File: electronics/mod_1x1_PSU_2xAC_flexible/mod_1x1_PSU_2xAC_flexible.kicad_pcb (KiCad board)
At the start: 2 copper layers, 42.5 x 46.2 mm, 56 parts, among them J1 module_2x15_left_input, J2 module_2x15_right_input, J3 Jack-DC, J4 Jack-DC, J5 Conn_01x02, J6 Conn_01x02, U1 LM317, U2 LM317, U3 LM337, U4 LM78XX

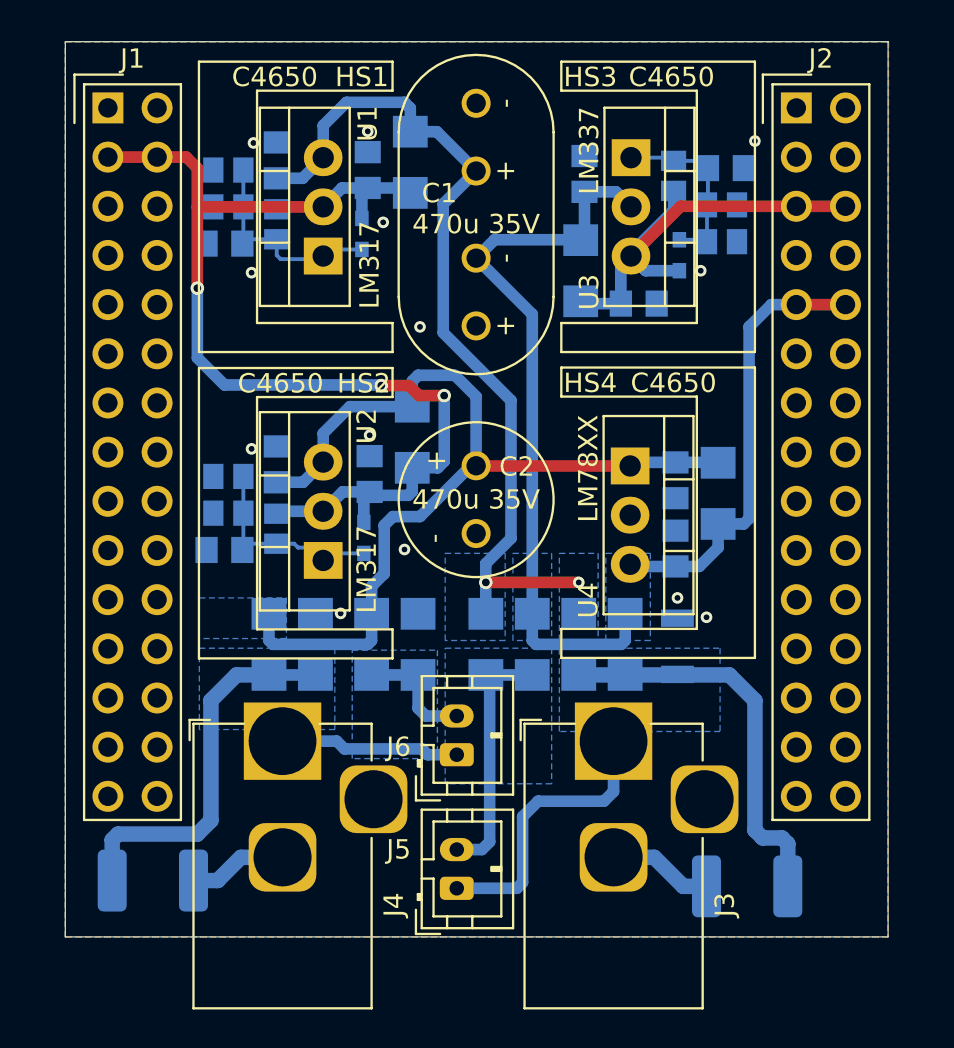
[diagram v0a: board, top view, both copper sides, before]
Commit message: updated PCB with newer/different footprints
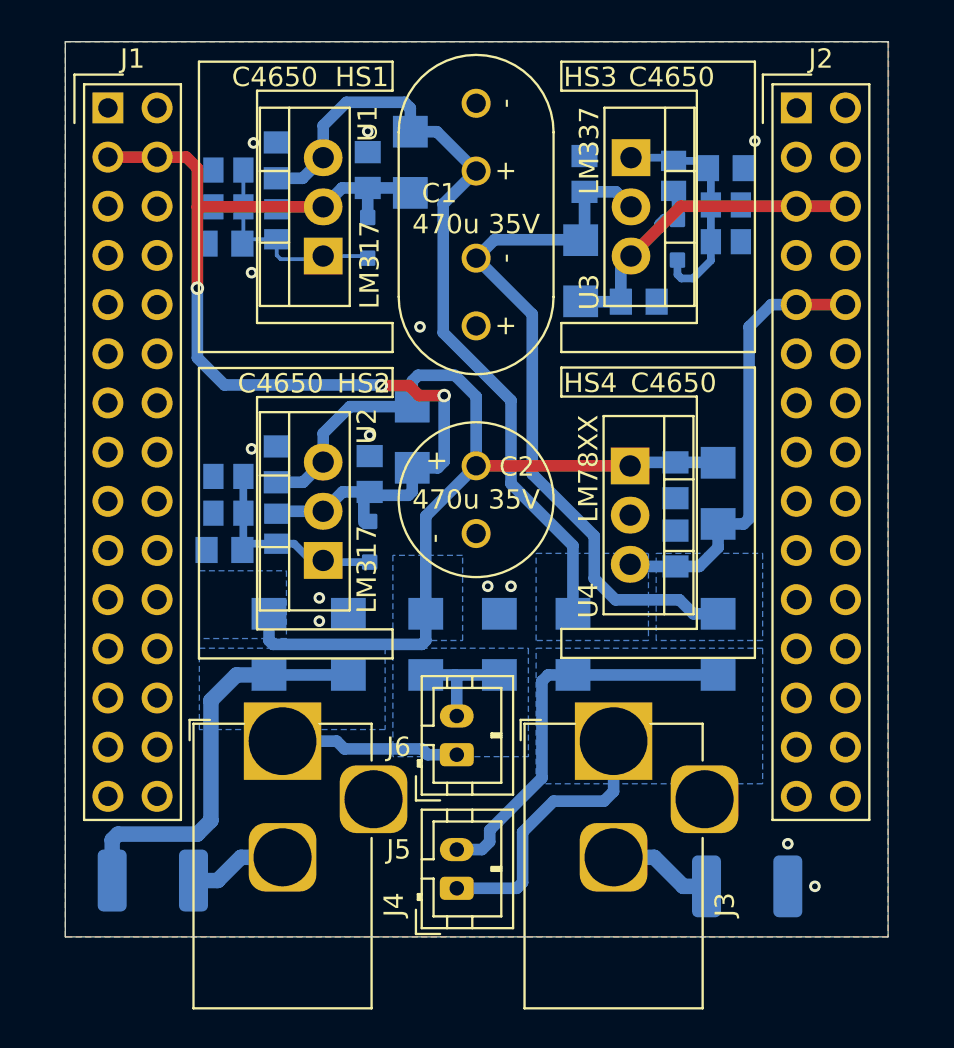
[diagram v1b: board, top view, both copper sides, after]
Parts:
- removed D3, D4: D, SquantorDiodes:SOD-123F-hand
- removed R1: R, SquantorRcl:R_1206
- D10, D12, D14: footprint SquantorDiodes:SOD-523_hand -> SquantorDiodes:SOD-323-nexperia-hand
- N1: value 20220716 -> 202200917
- moved D2 9.60 mm to (176.3, 100.1)
- moved D1 4.50 mm to (168.8, 100.1)
- moved D6 4.20 mm to (165.0, 100.1)
- moved D5 2.80 mm to (161.2, 100.1)
- moved D8 1.70 mm to (157.2, 100.1)
- moved D12 0.81 mm to (174.2, 79.2), turned to 90 degrees
- moved D14 0.36 mm to (158.3, 94.8)
- moved D10 0.36 mm to (158.2, 79.1)
- moved R5 0.20 mm to (176.7, 77.4)
- moved R6 0.20 mm to (176.7, 79.3)
- moved C11 0.10 mm to (172.2, 82.4)
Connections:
- F2 pad 2: /AC1_NEUT -> GND
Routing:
- net /AC1_NEUT: track 20.5 -> 0.00 mm
- net /AC1_PHASE: track 13.0 -> 20.5 mm
- net /DC1p: track 45.4 -> 41.4 mm, vias 2 -> 0
- net Net-(D12-K): track 9.49 -> 12.0 mm
- net /V-A: track 24.0 -> 21.6 mm
- net /AC2_NEUT: track 19.8 -> 21.5 mm
- net /DC1n: track 38.4 -> 37.3 mm
- net /DC2: track 50.0 -> 50.6 mm
- removed copper zone on B.Cu, net /AC1_NEUT

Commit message: small changes for producability and form and fit
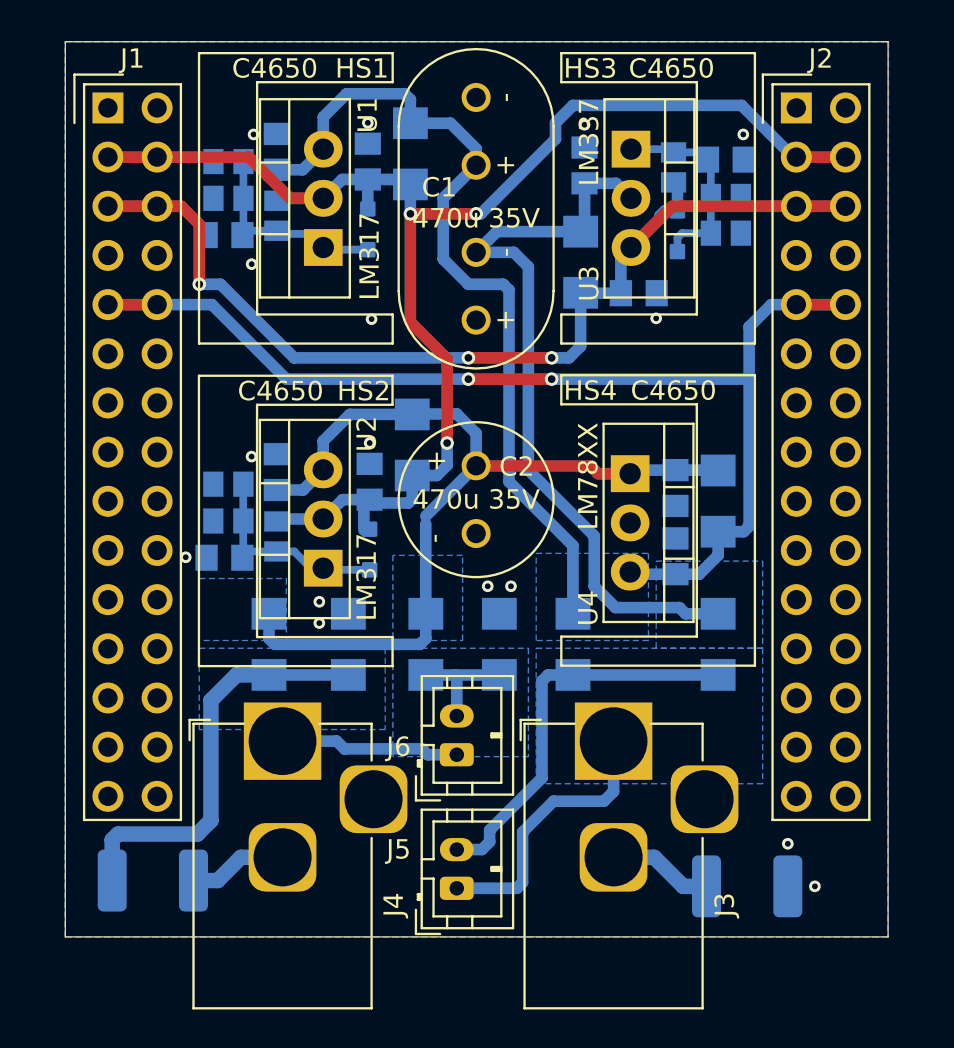
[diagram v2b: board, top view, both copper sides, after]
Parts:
- N1: value 202200917 -> 202201025
- moved C4 0.44 mm to (150.8, 79.0)
- moved R4 0.44 mm to (153.5, 78.0)
- moved C9 0.44 mm to (158.2, 75.2)
- moved D10 0.44 mm to (158.2, 78.7)
- moved HS1 0.44 mm to (154.5, 77.1)
- moved C3 0.44 mm to (153.5, 74.7)
- moved D9 0.44 mm to (160.4, 74.8)
- moved R2 0.44 mm to (151.0, 77.1)
- moved R3 0.44 mm to (151.0, 75.2)
- moved U1 0.44 mm to (155.9, 77.1)
- moved C11 0.44 mm to (172.2, 82.0)
- moved R5 0.44 mm to (176.7, 77.0)
- moved R7 0.44 mm to (174.0, 75.5)
- moved C5 0.44 mm to (169.4, 75.4)
- moved C6 0.44 mm to (176.7, 75.1)
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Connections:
- J1 pad 10: unconnected-(J1-+5V-Pad10) -> /+5V
- J1 pad 5: unconnected-(J1--VA-Pad5) -> /V-A
- J1 pad 6: unconnected-(J1--VA-Pad6) -> /V-A
- J1 pad 9: unconnected-(J1-+5V-Pad9) -> /+5V
- J2 pad 3: unconnected-(J2-+VA-Pad3) -> /V+A
- J2 pad 4: unconnected-(J2-+VA-Pad4) -> /V+A
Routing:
- net /+5V: track 23.3 -> 58.4 mm, vias 0 -> 2
- net /V-A: track 21.6 -> 53.9 mm, vias 0 -> 3
- net /V+A: track 59.4 -> 75.2 mm
- net /DC2: track 50.6 -> 46.5 mm
- net /DC1p: track 41.4 -> 43.7 mm
- net /DC1n: track 37.3 -> 39.4 mm
- net Net-(D12-K): track 12.0 -> 10.6 mm
- net Net-(D10-A): track 11.4 -> 10.8 mm
- net GND: vias 13 -> 16

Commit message: updated components and fixed warnings
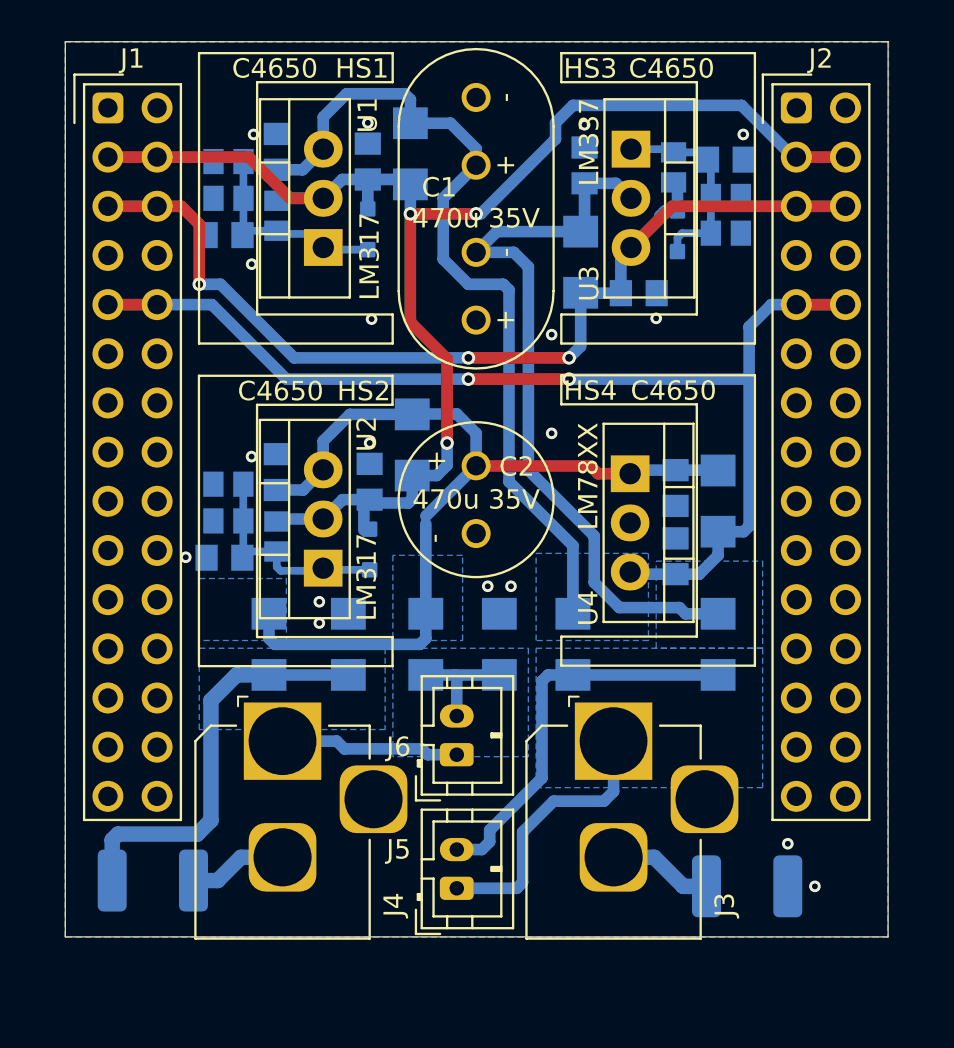
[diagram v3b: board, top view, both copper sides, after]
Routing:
- net Net-(D14-A): track 10.9 -> 11.5 mm
- net GND: vias 16 -> 18

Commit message: imported aisler budget design rules, fixed all DRC errors resulting from that
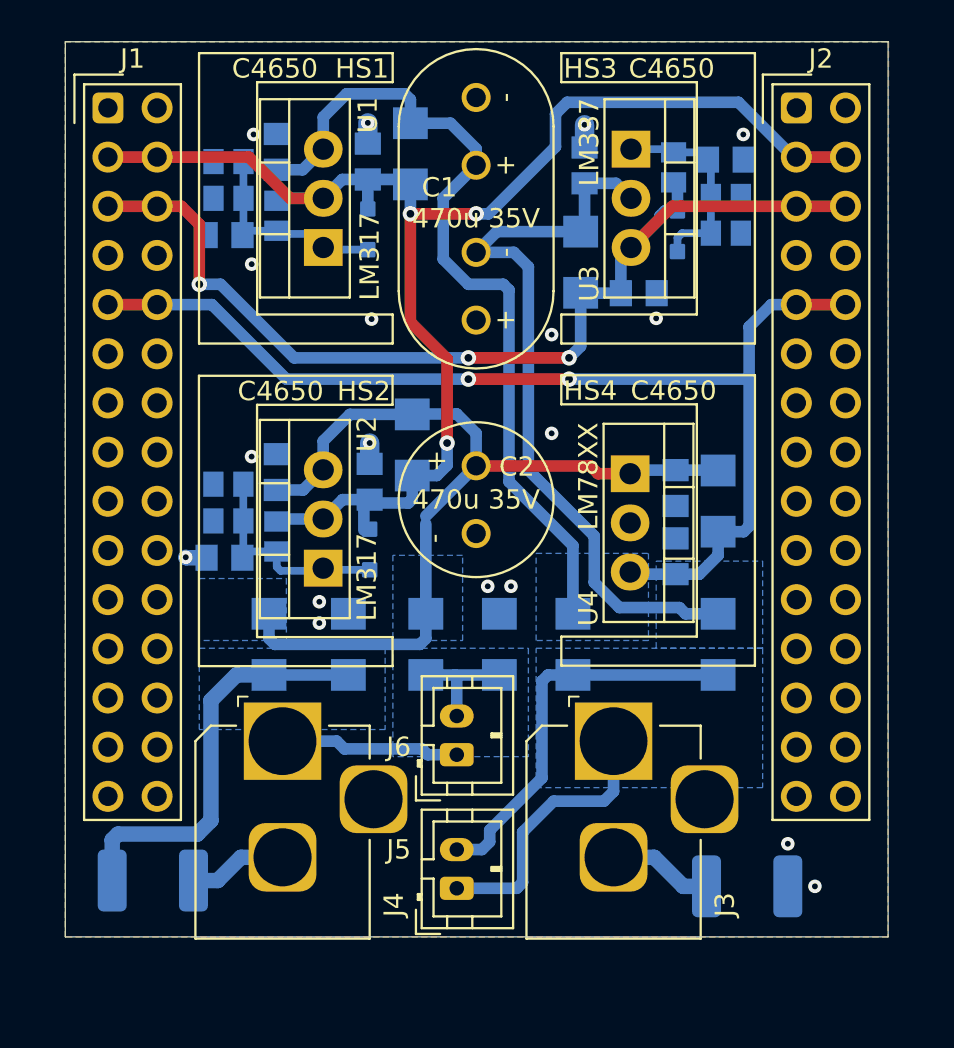
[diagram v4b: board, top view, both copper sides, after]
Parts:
- N1: value 202201025 -> 20231208
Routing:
- net GND: track 0.00 -> 4.41 mm
- net /V+A: track 75.2 -> 75.9 mm
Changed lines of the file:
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@@
         (effects (font (size 1 1) (thickness 0.15)) (justify mirror))
     )
-    (fp_text value "202201025" (at 0 0) (layer "B.SilkS")
+    (fp_text value "20231208" (at 0 0) (layer "B.SilkS")
         (effects (font (size 0.8 0.8) (thickness 0.15)) (justify mirror))
     )
@@
   (gr_rect (start 142.58 68.97) (end 185.08 115.21)
     (stroke (width 0.05) (type solid)) (fill none) (layer "Edge.Cuts"))
-  (via (at 158.3 89.7) (size 0.6) (drill 0.3) (layers "F.Cu" "B.Cu") (free) (net 1))
-  (via (at 169.4 73.26) (size 0.6) (drill 0.3) (layers "F.Cu" "B.Cu") (free) (net 1))
-  (via (at 158.4 83.3) (size 0.6) (drill 0.3) (layers "F.Cu" "B.Cu") (free) (net 1))
-  (via (at 167.7 89.2) (size 0.6) (drill 0.3) (layers "F.Cu" "B.Cu") (free) (net 1))
-  (via (at 158.205 73.16) (size 0.6) (drill 0.3) (layers "F.Cu" "B.Cu") (free) (net 1))
-  (via (at 165.6 97.1) (size 0.6) (drill 0.3) (layers "F.Cu" "B.Cu") (free) (net 1))
-  (via (at 155.7 99) (size 0.6) (drill 0.3) (layers "F.Cu" "B.Cu") (free) (net 1))
-  (via (at 173.1 83.26) (size 0.6) (drill 0.3) (layers "F.Cu" "B.Cu") (free) (net 1))
-  (via (at 179.9 110.4) (size 0.6) (drill 0.3) (layers "F.Cu" "B.Cu") (free) (net 1))
-  (via (at 152.305 73.76) (size 0.6) (drill 0.3) (layers "F.Cu" "B.Cu") (free) (net 1))
-  (via (at 167.7 84.1) (size 0.6) (drill 0.3) (layers "F.Cu" "B.Cu") (free) (net 1))
-  (via (at 164.4 97.1) (size 0.6) (drill 0.3) (layers "F.Cu" "B.Cu") (free) (net 1))
-  (via (at 152.2 90.4) (size 0.6) (drill 0.3) (layers "F.Cu" "B.Cu") (free) (net 1))
-  (via (at 155.7 97.9) (size 0.6) (drill 0.3) (layers "F.Cu" "B.Cu") (free) (net 1))
-  (via (at 152.205 80.46) (size 0.6) (drill 0.3) (layers "F.Cu" "B.Cu") (free) (net 1))
-  (via (at 148.8 95.6) (size 0.6) (drill 0.3) (layers "F.Cu" "B.Cu") (free) (net 1))
-  (via (at 181.3 112.6) (size 0.6) (drill 0.3) (layers "F.Cu" "B.Cu") (free) (net 1))
-  (via (at 177.6 73.76) (size 0.6) (drill 0.3) (layers "F.Cu" "B.Cu") (free) (net 1))
+  (via (at 158.3 89.7) (size 0.7) (drill 0.3) (layers "F.Cu" "B.Cu") (free) (net 1))
+  (via (at 169.4 73.26) (size 0.7) (drill 0.3) (layers "F.Cu" "B.Cu") (free) (net 1))
+  (via (at 158.4 83.3) (size 0.7) (drill 0.3) (layers "F.Cu" "B.Cu") (free) (net 1))
+  (via (at 167.7 89.2) (size 0.7) (drill 0.3) (layers "F.Cu" "B.Cu") (free) (net 1))
+  (via (at 158.205 73.16) (size 0.7) (drill 0.3) (layers "F.Cu" "B.Cu") (free) (net 1))
+  (via (at 165.6 97.1) (size 0.7) (drill 0.3) (layers "F.Cu" "B.Cu") (free) (net 1))
+  (via (at 155.7 99) (size 0.7) (drill 0.3) (layers "F.Cu" "B.Cu") (free) (net 1))
+  (via (at 173.1 83.26) (size 0.7) (drill 0.3) (layers "F.Cu" "B.Cu") (free) (net 1))
+  (via (at 179.9 110.4) (size 0.7) (drill 0.3) (layers "F.Cu" "B.Cu") (free) (net 1))
+  (via (at 152.305 73.76) (size 0.7) (drill 0.3) (layers "F.Cu" "B.Cu") (free) (net 1))
+  (via (at 167.7 84.1) (size 0.7) (drill 0.3) (layers "F.Cu" "B.Cu") (free) (net 1))
+  (via (at 164.4 97.1) (size 0.7) (drill 0.3) (layers "F.Cu" "B.Cu") (free) (net 1))
+  (via (at 152.2 90.4) (size 0.7) (drill 0.3) (layers "F.Cu" "B.Cu") (free) (net 1))
+  (via (at 155.7 97.9) (size 0.7) (drill 0.3) (layers "F.Cu" "B.Cu") (free) (net 1))
+  (via (at 152.205 80.46) (size 0.7) (drill 0.3) (layers "F.Cu" "B.Cu") (free) (net 1))
+  (via (at 148.8 95.6) (size 0.7) (drill 0.3) (layers "F.Cu" "B.Cu") (free) (net 1))
+  (via (at 181.3 112.6) (size 0.7) (drill 0.3) (layers "F.Cu" "B.Cu") (free) (net 1))
+  (via (at 177.6 73.76) (size 0.7) (drill 0.3) (layers "F.Cu" "B.Cu") (free) (net 1))
+  (segment (start 149.875 95.625) (end 148.825 95.625) (width 0.8) (layer "B.Cu") (net 1))
+  (segment (start 148.825 95.625) (end 148.8 95.6) (width 0.8) (layer "B.Cu") (net 1))
+  (segment (start 158.205 74.235) (end 158.205 73.16) (width 1) (layer "B.Cu") (net 1))
+  (segment (start 169.4 74.435) (end 169.4 73.26) (width 1) (layer "B.Cu") (net 1))
+  (segment (start 158.3 90.775) (end 158.3 89.7) (width 1) (layer "B.Cu") (net 1))
   (segment (start 182.88 82.55) (end 180.34 82.55) (width 0.6) (layer "F.Cu") (net 2))
   (segment (start 168.6 86.4) (end 163.4 86.4) (width 0.6) (layer "F.Cu") (net 2))
   (segment (start 147.32 82.55) (end 144.78 82.55) (width 0.6) (layer "F.Cu") (net 2))
-  (via (at 163.4 86.4) (size 0.7) (drill 0.4) (layers "F.Cu" "B.Cu") (net 2))
-  (via (at 168.6 86.4) (size 0.7) (drill 0.4) (layers "F.Cu" "B.Cu") (net 2))
+  (via (at 163.4 86.4) (size 0.8) (drill 0.4) (layers "F.Cu" "B.Cu") (net 2))
+  (via (at 168.6 86.4) (size 0.8) (drill 0.4) (layers "F.Cu" "B.Cu") (net 2))
   (segment (start 163.4 86.4) (end 154 86.4) (width 0.6) (layer "B.Cu") (net 2))
   (segment (start 177.62 94.28) (end 177.9 94) (width 0.6) (layer "B.Cu") (net 2))
@@
   (segment (start 144.78 74.93) (end 147.32 74.93) (width 0.6) (layer "F.Cu") (net 31))
   (segment (start 154.190786 77.06) (end 155.905 77.06) (width 0.6) (layer "F.Cu") (net 31))
-  (via (at 163.8 77.86) (size 0.7) (drill 0.4) (layers "F.Cu" "B.Cu") (net 31))
-  (via (at 162.3 89.7) (size 0.7) (drill 0.4) (layers "F.Cu" "B.Cu") (net 31))
-  (via (at 160.405 77.86) (size 0.7) (drill 0.4) (layers "F.Cu" "B.Cu") (net 31))
+  (via (at 163.8 77.86) (size 0.8) (drill 0.4) (layers "F.Cu" "B.Cu") (net 31))
+  (via (at 162.3 89.7) (size 0.8) (drill 0.4) (layers "F.Cu" "B.Cu") (net 31))
+  (via (at 160.405 77.86) (size 0.8) (drill 0.4) (layers "F.Cu" "B.Cu") (net 31))
+  (segment (start 164.44 77.86) (end 167.9 74.4) (width 0.6) (layer "B.Cu") (net 31))
   (segment (start 153.63 77.06) (end 153.505 77.185) (width 0.6) (layer "B.Cu") (net 31))
   (segment (start 156.9 92.625) (end 155.9 93.625) (width 0.6) (layer "B.Cu") (net 31))
+  (segment (start 177.354214 72.1) (end 180.184214 74.93) (width 0.6) (layer "B.Cu") (net 31))
   (segment (start 160.405 77.86) (end 160.405 76.34) (width 0.6) (layer "B.Cu") (net 31))
   (segment (start 161.77 91.38) (end 160.5 91.38) (width 0.6) (layer "B.Cu") (net 31))
-  (segment (start 180.184214 74.93) (end 180.34 74.93) (width 0.6) (layer "B.Cu") (net 31))
-  (segment (start 167.9 73.16) (end 168.8 72.26) (width 0.6) (layer "B.Cu") (net 31))
-  (segment (start 164.04 77.86) (end 167.9 74) (width 0.6) (layer "B.Cu") (net 31))
-  (segment (start 163.8 77.86) (end 164.04 77.86) (width 0.6) (layer "B.Cu") (net 31))
   (segment (start 160.15 76.085) (end 160.405 76.34) (width 0.6) (layer "B.Cu") (net 31))
   (segment (start 158.205 76.085) (end 156.88 76.085) (width 0.6) (layer "B.Cu") (net 31))
   (segment (start 155.905 77.06) (end 153.63 77.06) (width 0.6) (layer "B.Cu") (net 31))
   (segment (start 160.3 92.8) (end 158.475 92.8) (width 0.6) (layer "B.Cu") (net 31))
-  (segment (start 168.8 72.26) (end 177.514214 72.26) (width 0.6) (layer "B.Cu") (net 31))
-  (segment (start 167.9 74) (end 167.9 73.16) (width 0.6) (layer "B.Cu") (net 31))
+  (segment (start 167.9 72.7) (end 168.5 72.1) (width 0.6) (layer "B.Cu") (net 31))
+  (segment (start 168.5 72.1) (end 177.354214 72.1) (width 0.6) (layer "B.Cu") (net 31))
+  (segment (start 180.184214 74.93) (end 180.34 74.93) (width 0.6) (layer "B.Cu") (net 31))
   (segment (start 158.205 76.085) (end 160.15 76.085) (width 0.6) (layer "B.Cu") (net 31))
+  (segment (start 163.8 77.86) (end 164.44 77.86) (width 0.6) (layer "B.Cu") (net 31))
   (segment (start 158.3 92.625) (end 156.9 92.625) (width 0.6) (layer "B.Cu") (net 31))
   (segment (start 158 92.925) (end 158.3 92.625) (width 0.6) (layer "B.Cu") (net 31))
   (segment (start 155.9 93.625) (end 153.625 93.625) (width 0.6) (layer "B.Cu") (net 31))
-  (segment (start 177.514214 72.26) (end 180.184214 74.93) (width 0.6) (layer "B.Cu") (net 31))
   (segment (start 160.5 91.38) (end 160.5 92.6) (width 0.6) (layer "B.Cu") (net 31))
   (segment (start 156.88 76.085) (end 155.905 77.06) (width 0.6) (layer "B.Cu") (net 31))
@@
   (segment (start 153.625 93.625) (end 153.5 93.75) (width 0.6) (layer "B.Cu") (net 31))
   (segment (start 158.205 77.61) (end 158.205 76.085) (width 0.6) (layer "B.Cu") (net 31))
+  (segment (start 167.9 74.4) (end 167.9 72.7) (width 0.6) (layer "B.Cu") (net 31))
   (segment (start 162.3 90.85) (end 161.77 91.38) (width 0.6) (layer "B.Cu") (net 31))
   (segment (start 162.3 89.7) (end 162.3 90.85) (width 0.6) (layer "B.Cu") (net 31))
@@
   (segment (start 163.4 85.300497) (end 168.599503 85.300497) (width 0.6) (layer "F.Cu") (net 32))
   (segment (start 149.5 78.4) (end 148.57 77.47) (width 0.6) (layer "F.Cu") (net 32))
-  (via (at 168.599503 85.300497) (size 0.7) (drill 0.4) (layers "F.Cu" "B.Cu") (net 32))
-  (via (at 149.5 81.5) (size 0.7) (drill 0.4) (layers "F.Cu" "B.Cu") (net 32))
-  (via (at 163.4 85.300497) (size 0.7) (drill 0.4) (layers "F.Cu" "B.Cu") (net 32))
+  (via (at 168.599503 85.300497) (size 0.8) (drill 0.4) (layers "F.Cu" "B.Cu") (net 32))
+  (via (at 149.5 81.5) (size 0.8) (drill 0.4) (layers "F.Cu" "B.Cu") (net 32))
+  (via (at 163.4 85.300497) (size 0.8) (drill 0.4) (layers "F.Cu" "B.Cu") (net 32))
   (segment (start 171.275 81.96) (end 169.22 81.96) (width 0.6) (layer "B.Cu") (net 32))
   (segment (start 169.2 84.7) (end 169.2 81.94) (width 0.6) (layer "B.Cu") (net 32))
